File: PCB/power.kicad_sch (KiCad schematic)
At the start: 0 parts

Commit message: added reference schematic for nrf52820 and placed components for power
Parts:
- added BT1: Battery_Cell, symbol Device:Battery_Cell
- added Q1, Q2: NMOS, symbol Simulation_SPICE:NMOS
- added U2: BQ297xy, Package_SON:WSON-6_1.5x1.5mm_P0.5mm, symbol Battery_Management:BQ297xy
- added U3: BQ24090DGQ, Package_SO:HVSSOP-10-1EP_3x3mm_P0.5mm_EP1.57x1.88mm_ThermalVias, symbol Battery_Management:BQ24090DGQ
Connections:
- new net: U3.11 (VSS), U3.3 (VSS)

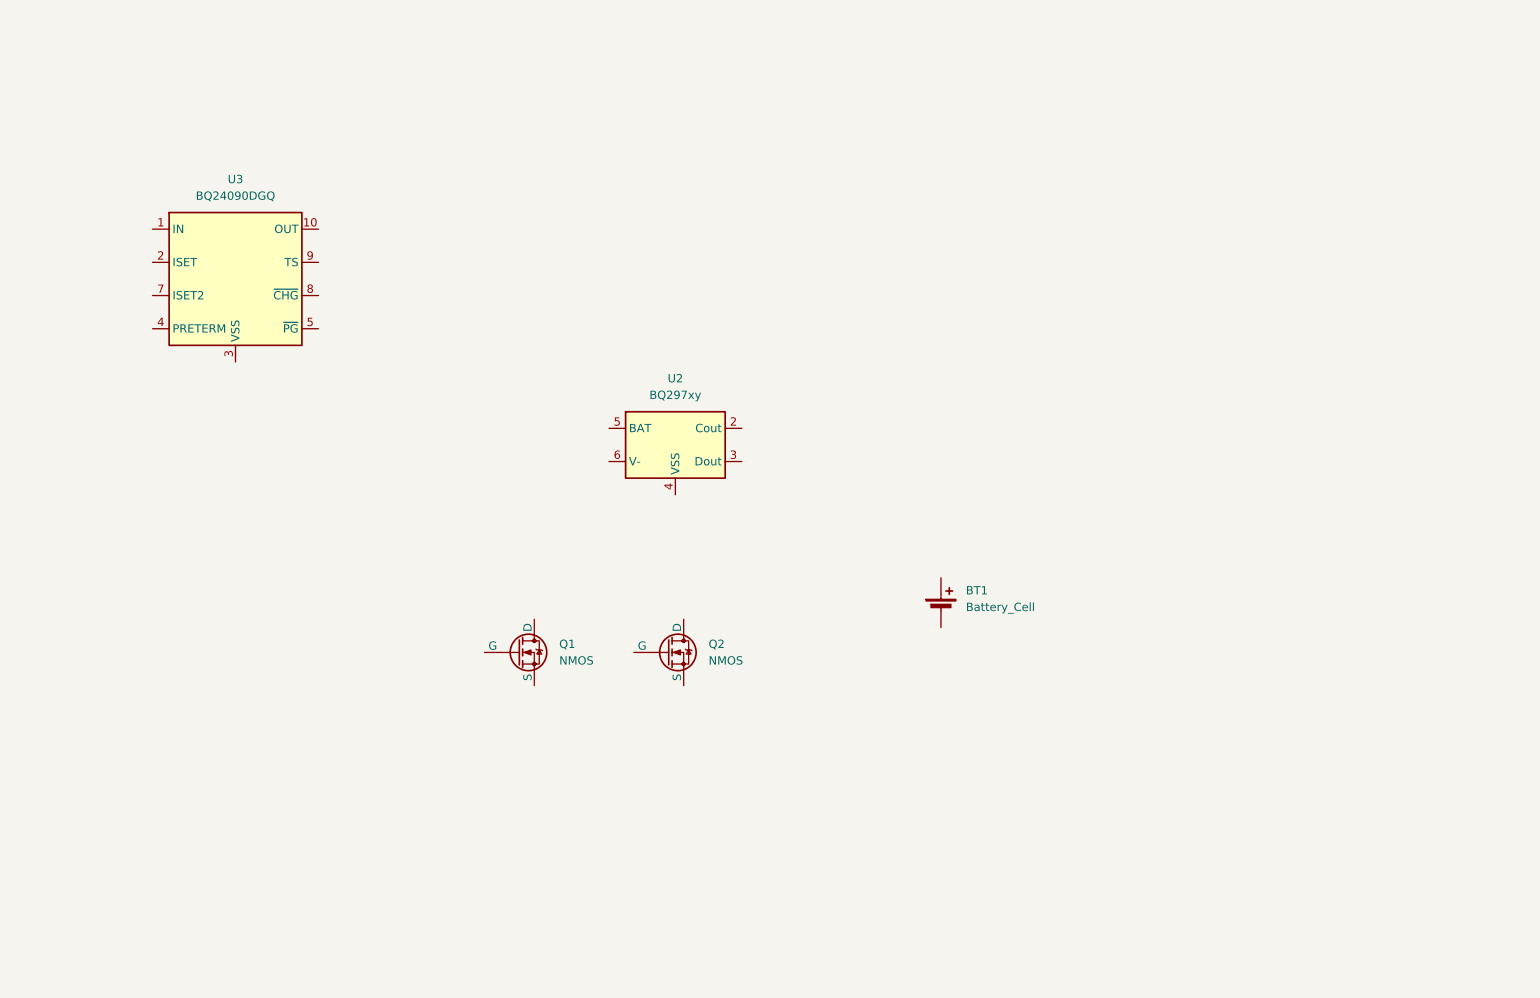
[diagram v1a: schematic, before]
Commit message: Added more power components
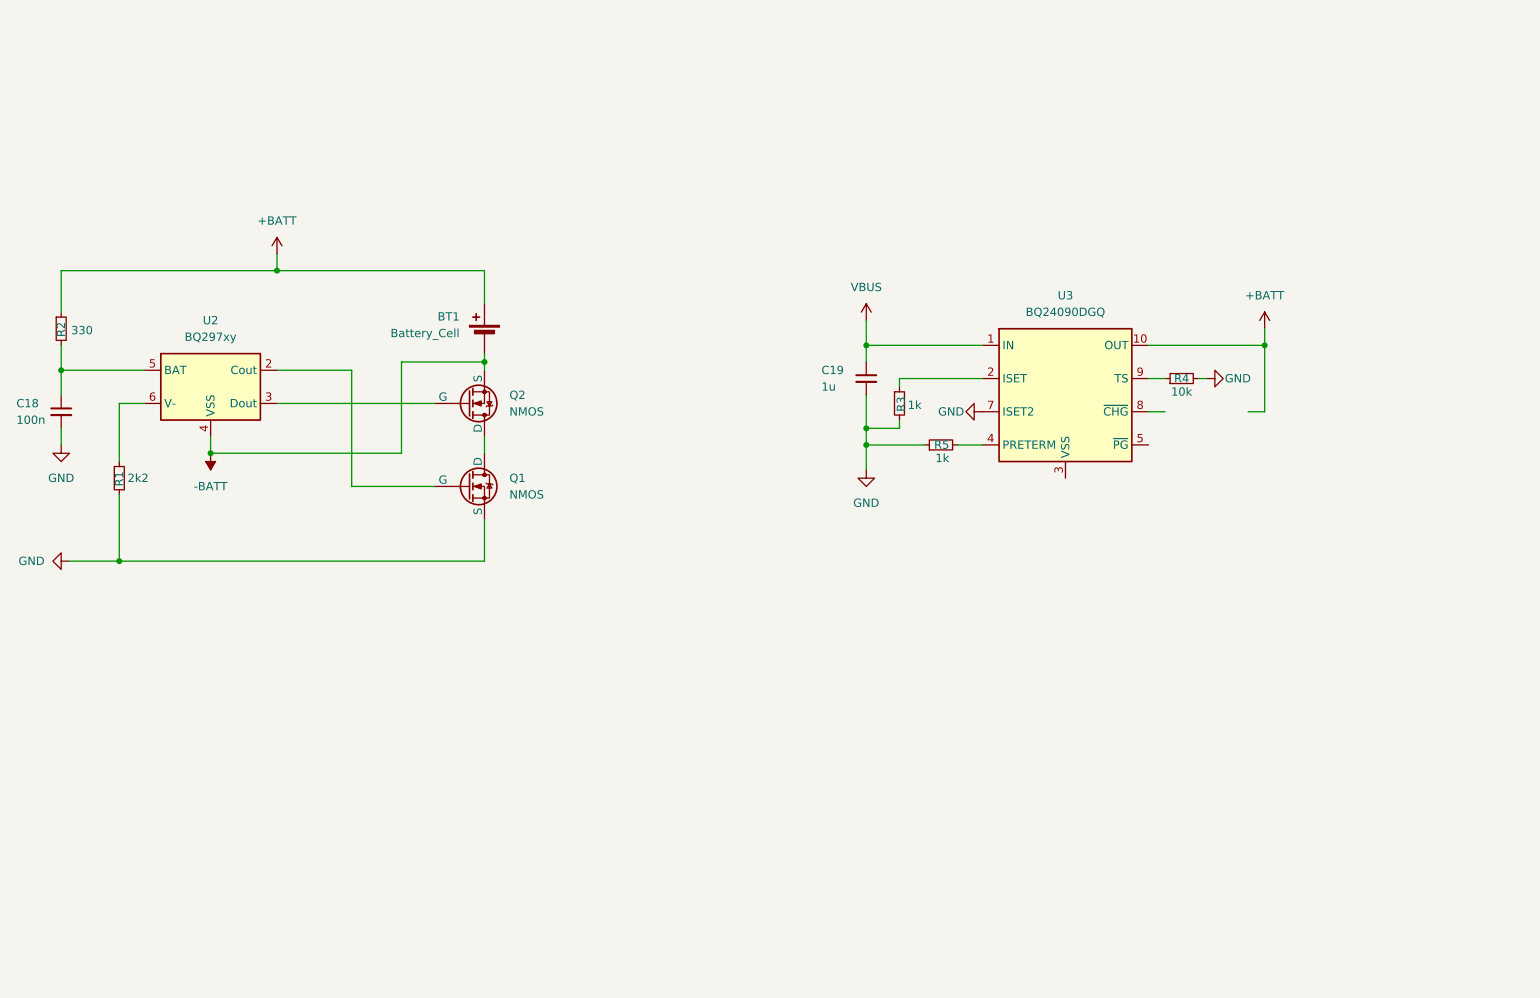
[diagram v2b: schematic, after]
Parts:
- added C18: 100n, symbol Device:C_Small
- added C19: 1u, symbol Device:C_Small
- added R1: 2k2, symbol Device:R_Small
- added R2: 330, symbol Device:R_Small
- added R3, R5: 1k, symbol Device:R_Small
- added R4: 10k, symbol Device:R_Small
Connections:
- net +BATT: now reaches BT1.1 (+)
- net +BATT: now also U3.10 (OUT), R2.1
- net -BATT: now reaches BT1.2 (-)
- net -BATT: now also Q2.3 (S), U2.4 (VSS)
- net at Q1.1 (D): now also Q2.1 (D)
- net at Q1.2 (G): now also U2.2 (Cout)
- net GND: now reaches Q1.3 (S)
- net GND: now also U3.7 (ISET2), C18.2, C19.2, R1.2, R3.2, R4.2, R5.1
- net at Q2.2 (G): now also U2.3 (Dout)
- net at U2.5 (BAT): now also C18.1, R2.2
- net at U2.6 (V-): now also R1.1
- net VBUS: now reaches U3.1 (IN)
- net VBUS: now also C19.1
- net at U3.2 (ISET): now also R3.1
- net at U3.4 (PRETERM): now also R5.2
- net at U3.9 (TS): now also R4.1
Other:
- moved on the sheet: BT1, Q1, Q2, U2, U3

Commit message: Added more components and added most needed values for the nrf example schematic
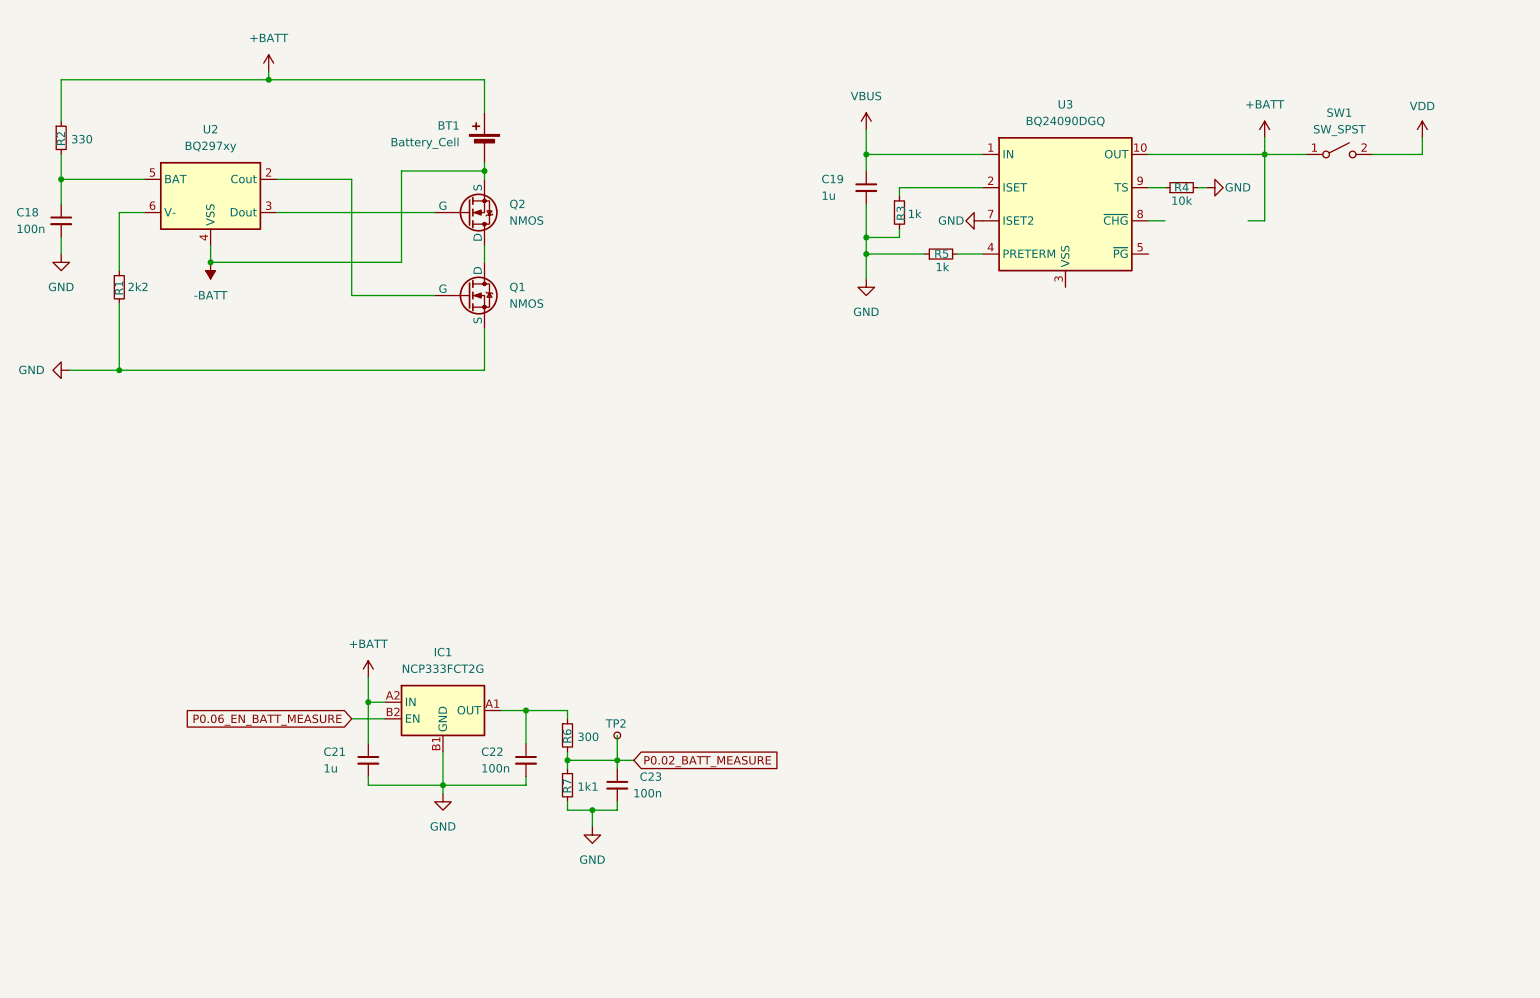
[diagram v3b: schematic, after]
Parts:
- added C21: 1u, Capacitor_SMD:C_0402_1005Metric, symbol Device:C_Small
- added C22, C23: 100n, Capacitor_SMD:C_0402_1005Metric, symbol Device:C_Small
- added IC1: NCP333FCT2G, BGA4C40P2X2_76X76X63, symbol NCP333FCT2G:NCP333FCT2G
- added R6: 300, Resistor_SMD:R_0402_1005Metric, symbol Device:R_Small
- added R7: 1k1, Resistor_SMD:R_0402_1005Metric, symbol Device:R_Small
- added SW1: SW_SPST, symbol Switch:SW_SPST
- added TP2: TestPoint_Small, TestPoint:TestPoint_Pad_D1.0mm, symbol Connector:TestPoint_Small
- C18: footprint (none) -> Capacitor_SMD:C_0402_1005Metric
- C19: footprint (none) -> Capacitor_SMD:C_0603_1608Metric
- Q1, Q2: footprint (none) -> Package_TO_SOT_SMD:SOT-23
- R1, R2, R3, R4, R5: footprint (none) -> Resistor_SMD:R_0402_1005Metric
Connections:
- net +BATT: now also C21.1, IC1.A2 (IN), SW1.1 (A)
- net GND: now also C21.2, C22.2, C23.2, IC1.B1 (GND), R7.2
- new net: C22.1, IC1.A1 (OUT), R6.1
- new net P0.02_BATT_MEASURE: C23.1, R6.2, R7.1, TP2.1
- new net P0.06_EN_BATT_MEASURE: IC1.B2 (EN)
- new net VDD: SW1.2 (B)
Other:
- moved on the sheet: BT1, C18, C19, Q1, Q2, R1, R2, R3, R4, R5, U2, U3

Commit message: Added the Calathea Leaf as the outline and artwork for the project
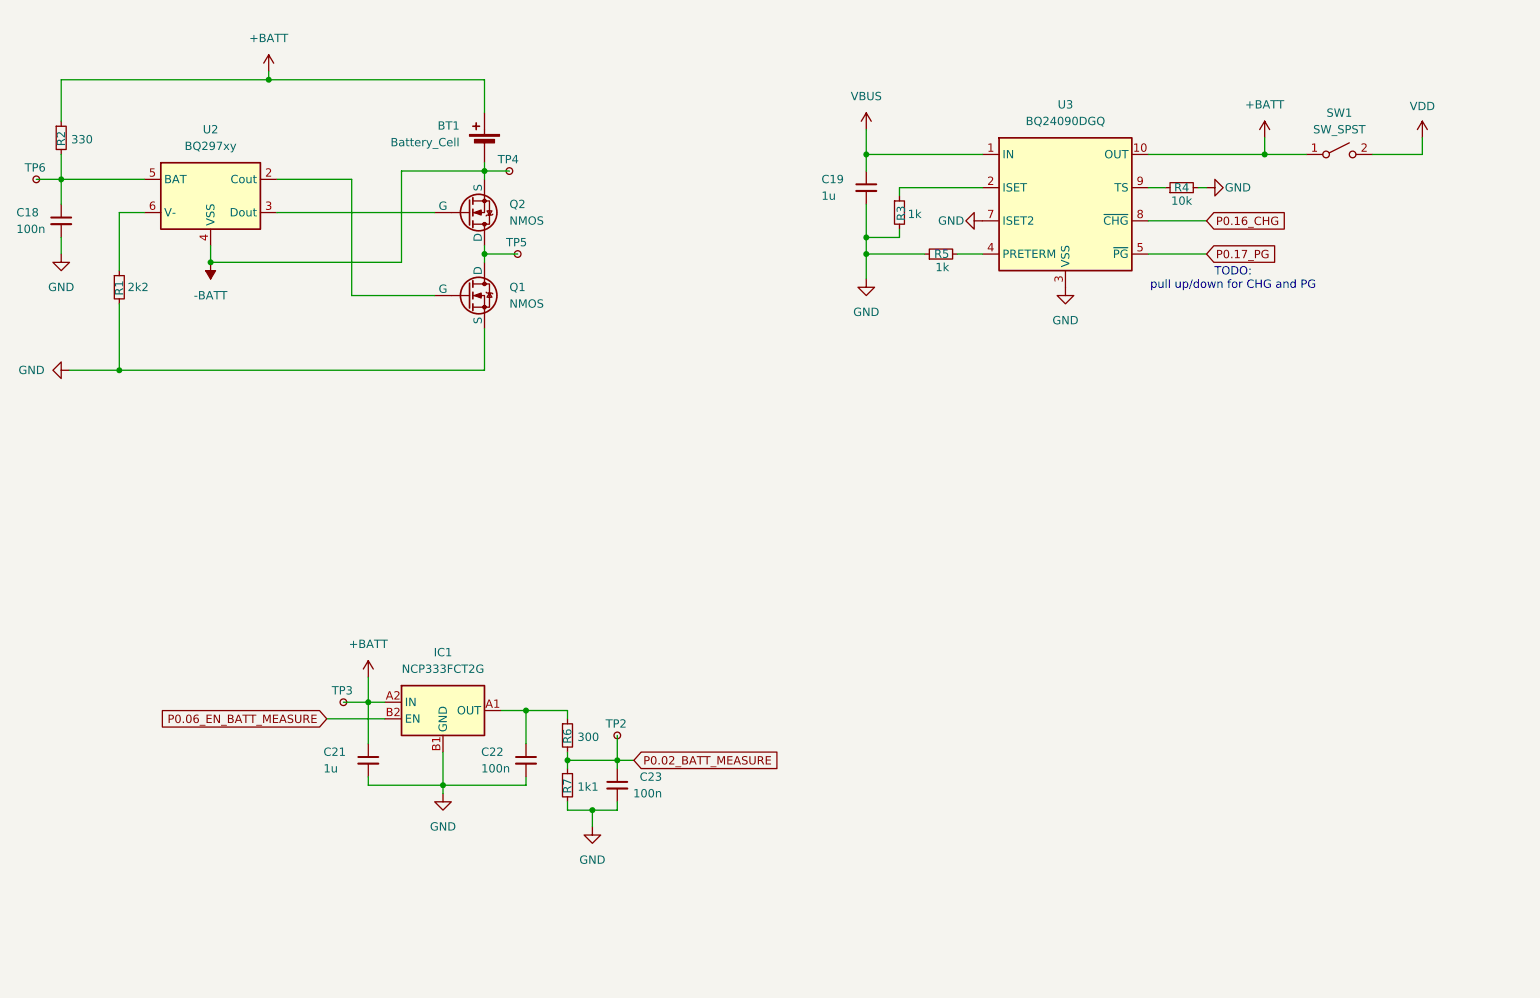
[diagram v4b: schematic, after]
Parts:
- added TP3, TP4, TP5, TP6: TestPoint_Small, TestPoint:TestPoint_Pad_D1.0mm, symbol Connector:TestPoint_Small
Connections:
- net +BATT: now also TP3.1
- net -BATT: now also TP4.1
- net GND: now also U3.11 (VSS), U3.3 (VSS)
- net at Q1.1 (D), Q2.1 (D): now also TP5.1
- net at C18.1, R2.2, U2.5 (BAT): now also TP6.1
- net P0.17_PG: now reaches U3.5 (~{PG})
- net P0.16_CHG: now reaches U3.8 (~{CHG})
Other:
- note added: "TODO: pull up/down for CHG and PG"

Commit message: added dcdc for external components. Changed board edge to a rect for easier dev board routuing.
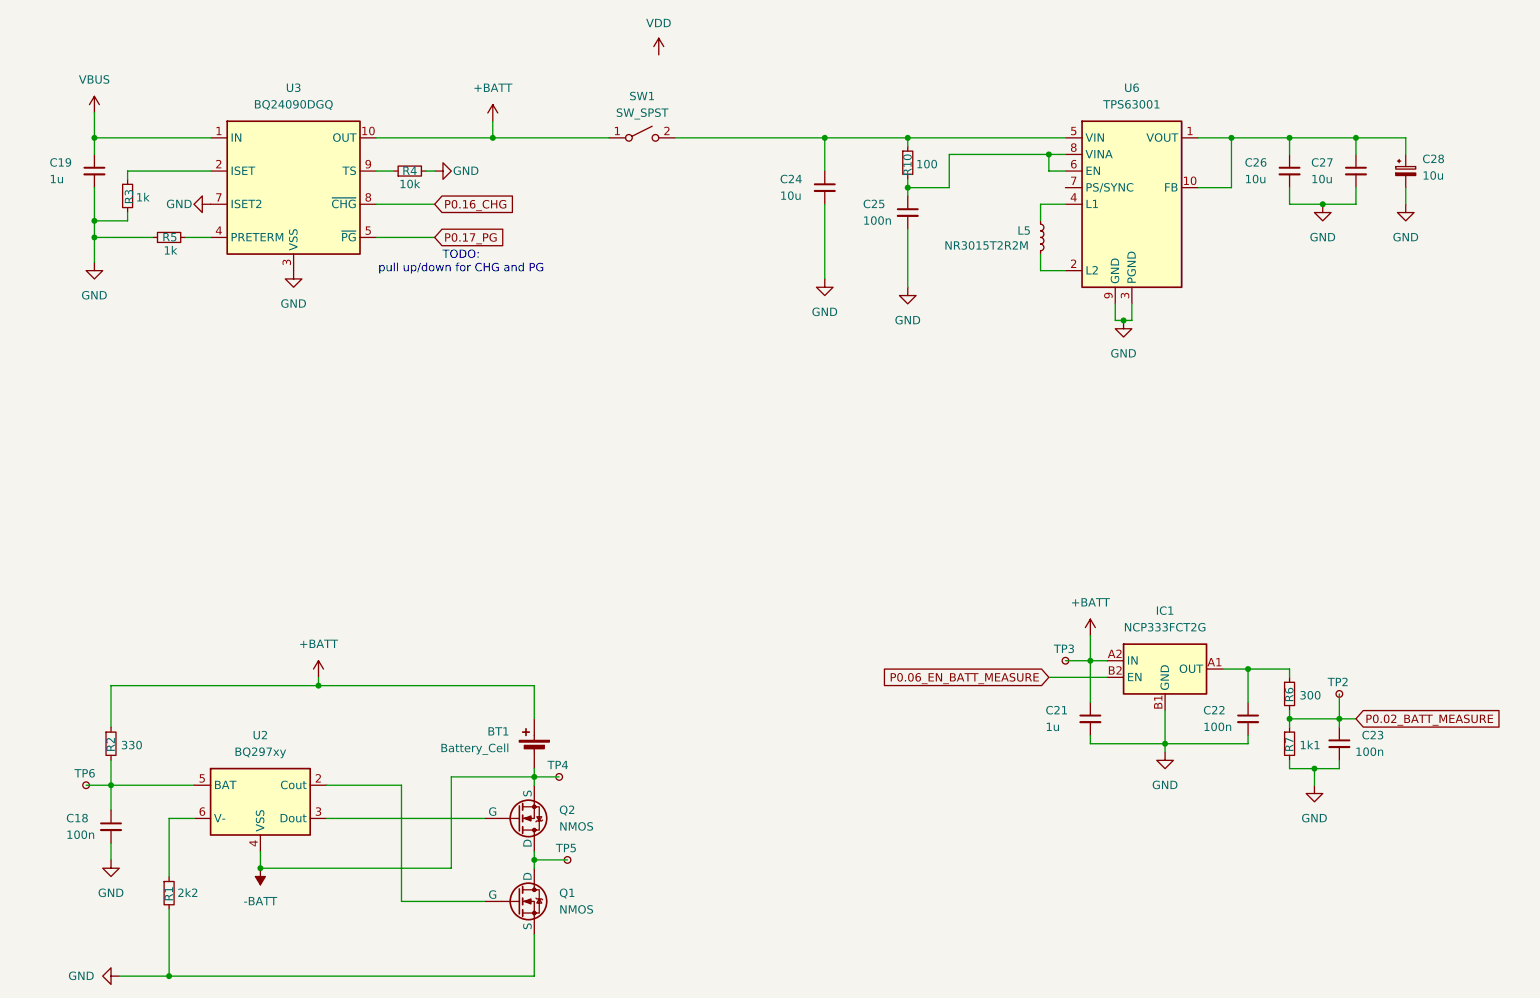
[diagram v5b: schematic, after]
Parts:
- added C24, C26, C27: 10u, Capacitor_SMD:C_0603_1608Metric, symbol Device:C_Small
- added C25: 100n, Capacitor_SMD:C_0603_1608Metric, symbol Device:C_Small
- added C28: 10u, symbol Device:C_Polarized_Small
- added L5: NR3015T2R2M, Inductor_SMD:L_Taiyo-Yuden_NR-30xx, symbol Device:L_Small
- added R10: 100, Resistor_SMD:R_0402_1005Metric, symbol Device:R_Small
- added U6: TPS63001, Package_SON:Texas_DRC0010J_ThermalVias, symbol Regulator_Switching:TPS63001
- BT1: footprint (none) -> Connector_JST:JST_PH_B2B-PH-SM4-TB_1x02-1MP_P2.00mm_Vertical
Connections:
- net GND: now also C24.2, C25.2, C26.2, C27.2, C28.2, U6.11 (PGND), U6.3 (PGND), U6.9 (GND)
- net VDD: no longer SW1.2 (B)
- new net: L5.1, U6.4 (L1)
- new net: L5.2, U6.2 (L2)
- new net: C26.1, C27.1, C28.1, U6.1 (VOUT), U6.10 (FB)
- new net: C24.1, R10.1, SW1.2 (B), U6.5 (VIN)
- new net: C25.1, R10.2, U6.6 (EN), U6.8 (VINA)
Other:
- moved on the sheet: BT1, C18, C19, C21, C22, C23, IC1, Q1, Q2, R1, R2, R3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
